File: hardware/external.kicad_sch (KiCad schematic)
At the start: 0 parts

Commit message: :sparkles: external board design
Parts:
- added PC1: ~, KeysDock:POGOPIN-8P-HS, symbol components:POGOPIN-8P-HS
- added R1, R2: 4.7kΩ, KeysDock:R_0402, symbol components:0402,4.7kΩ
- added R3: 10kΩ, KeysDock:R_0402, symbol components:0402,10kΩ
- added R4: 0Ω, KeysDock:R_0402, symbol components:0402,0Ω
- added SW1, SW10, SW11, SW12, SW13, SW14, SW2, SW3, SW4, SW5, SW6, SW7, SW8, SW9: ~, KeysDock:KD-SINGLE-KEY, symbol components:KD_SINGLE_KEY
- added T1: ~, KeysDock:XL4067TS, symbol components:XL4067TS
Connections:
- new net: SW14.H3 (HE_VOUT), T1.2 (Y7)
- new net: SW1.H4 (HE_SLEEP), SW11.H4 (HE_SLEEP), SW13.H4 (HE_SLEEP), SW14.H4 (HE_SLEEP), SW3.H4 (HE_SLEEP), SW5.H4 (HE_SLEEP), SW7.H4 (HE_SLEEP), SW9.H4 (HE_SLEEP)
- new net: R3.2, SW1.H6 (HE_AWAKE), SW10.H6 (HE_AWAKE), SW11.H6 (HE_AWAKE), SW12.H6 (HE_AWAKE), SW13.H6 (HE_AWAKE), SW14.H6 (HE_AWAKE), SW2.H6 (HE_AWAKE), SW3.H6 (HE_AWAKE), SW4.H6 (HE_AWAKE), SW5.H6 (HE_AWAKE), SW6.H6 (HE_AWAKE), SW7.H6 (HE_AWAKE), SW8.H6 (HE_AWAKE), SW9.H6 (HE_AWAKE)
- new net: SW8.H3 (HE_VOUT), T1.19 (Y12)
- new net: SW10.H4 (HE_SLEEP), SW12.H4 (HE_SLEEP), SW2.H4 (HE_SLEEP), SW4.H4 (HE_SLEEP), SW6.H4 (HE_SLEEP), SW8.H4 (HE_SLEEP)
- new net: SW7.H3 (HE_VOUT), T1.6 (Y3)
- new net: R1.1, T1.22 (Y9)
- new net: SW11.H3 (HE_VOUT), T1.4 (Y5)
- new net: SW9.H3 (HE_VOUT), T1.5 (Y4)
- new net: SW2.H3 (HE_VOUT), T1.16 (Y15)
- new net: SW4.H3 (HE_VOUT), T1.17 (Y14)
- new net: SW6.H3 (HE_VOUT), T1.18 (Y13)
- new net: SW10.H3 (HE_VOUT), T1.20 (Y11)
- new net: SW12.H3 (HE_VOUT), T1.21 (Y10)
- new net: R2.1, T1.23 (Y8)
- new net: SW13.H3 (HE_VOUT), T1.3 (Y6)
- new net: SW5.H3 (HE_VOUT), T1.7 (Y2)
- new net: SW3.H3 (HE_VOUT), T1.8 (Y1)
- new net: SW1.H3 (HE_VOUT), T1.9 (Y0)
- new net KEYS_ADC_OUT: PC1.3 (Y3), T1.1 (Z)
- new net KEYS_CH_A: PC1.5 (Y5), T1.10 (A)
- new net KEYS_CH_B: PC1.6 (Y6), T1.11 (B)
- new net KEYS_CH_C: PC1.7 (Y7), T1.14 (C)
- new net KEYS_CH_CE: PC1.4 (Y4), T1.15 (E#)
- new net KEYS_CH_D: PC1.8 (Y8), T1.13 (D)
- new net P,+3.3: PC1.1 (Y1), R1.2, R2.2, R3.1, SW1.H1 (HE_V3.3), SW10.H1 (HE_V3.3), SW11.H1 (HE_V3.3), SW12.H1 (HE_V3.3), SW13.H1 (HE_V3.3), SW14.H1 (HE_V3.3), SW2.H1 (HE_V3.3), SW3.H1 (HE_V3.3), SW4.H1 (HE_V3.3), SW5.H1 (HE_V3.3), SW6.H1 (HE_V3.3), SW7.H1 (HE_V3.3), SW8.H1 (HE_V3.3), SW9.H1 (HE_V3.3), T1.24 (VCC)
- new net P,E: PC1.2 (Y2), R4.2, SW1.H2 (GND), SW1.H5 (GND), SW10.H2 (GND), SW10.H5 (GND), SW11.H2 (GND), SW11.H5 (GND), SW12.H2 (GND), SW12.H5 (GND), SW13.H2 (GND), SW13.H5 (GND), SW14.H2 (GND), SW14.H5 (GND), SW2.H2 (GND), SW2.H5 (GND), SW3.H2 (GND), SW3.H5 (GND), SW4.H2 (GND), SW4.H5 (GND), SW5.H2 (GND), SW5.H5 (GND), SW6.H2 (GND), SW6.H5 (GND), SW7.H2 (GND), SW7.H5 (GND), SW8.H2 (GND), SW8.H5 (GND), SW9.H2 (GND), SW9.H5 (GND), T1.12 (GND)
- new net P,GND: R4.1
- no-connect marks 0 -> 2
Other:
- note added: "GNDA"
- note added: "GNDD"
- note added: "GND_BAT"

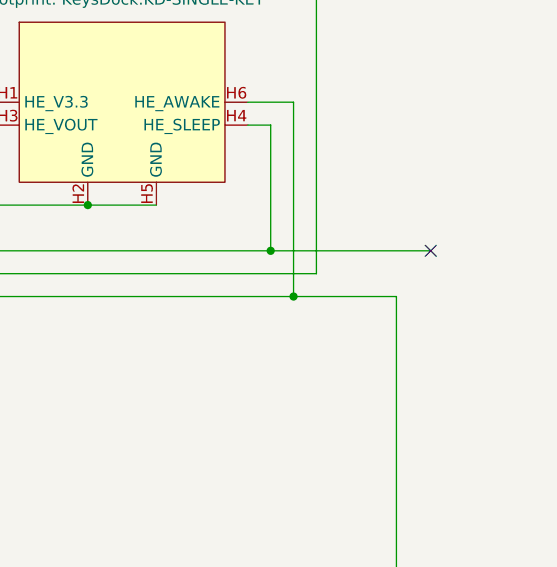
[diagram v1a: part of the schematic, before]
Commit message: :sparkles: finish pcb layout of controller
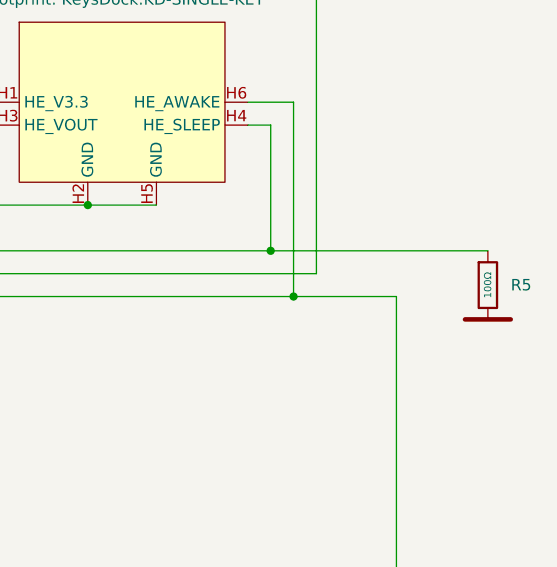
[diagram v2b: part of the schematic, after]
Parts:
- added R5: 100Ω, KeysDock:R_0402, symbol components:0402,100Ω
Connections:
- net P,E: now also R5.2; no longer SW1.H2 (GND), SW1.H5 (GND), SW10.H2 (GND), SW10.H5 (GND), SW11.H2 (GND), SW11.H5 (GND), SW12.H2 (GND), SW12.H5 (GND), SW13.H2 (GND), SW13.H5 (GND), SW14.H2 (GND), SW14.H5 (GND), SW2.H2 (GND), SW2.H5 (GND), SW3.H2 (GND), SW3.H5 (GND), SW4.H2 (GND), SW4.H5 (GND), SW5.H2 (GND), SW5.H5 (GND), SW6.H2 (GND), SW6.H5 (GND), SW7.H2 (GND), SW7.H5 (GND), SW8.H2 (GND), SW8.H5 (GND), SW9.H2 (GND), SW9.H5 (GND), T1.12 (GND)
- net P,GND: now also SW1.H2 (GND), SW1.H5 (GND), SW10.H2 (GND), SW10.H5 (GND), SW11.H2 (GND), SW11.H5 (GND), SW12.H2 (GND), SW12.H5 (GND), SW13.H2 (GND), SW13.H5 (GND), SW14.H2 (GND), SW14.H5 (GND), SW2.H2 (GND), SW2.H5 (GND), SW3.H2 (GND), SW3.H5 (GND), SW4.H2 (GND), SW4.H5 (GND), SW5.H2 (GND), SW5.H5 (GND), SW6.H2 (GND), SW6.H5 (GND), SW7.H2 (GND), SW7.H5 (GND), SW8.H2 (GND), SW8.H5 (GND), SW9.H2 (GND), SW9.H5 (GND), T1.12 (GND)
- net at SW1.H4 (HE_SLEEP), SW11.H4 (HE_SLEEP), SW13.H4 (HE_SLEEP)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: now also R5.1
- no-connect marks 2 -> 1

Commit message: :sparkles: finish all hardware designs
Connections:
- net at R5.1, SW1.H4 (HE_SLEEP), SW11.H4 (HE_SLEEP)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: now also SW10.H4 (HE_SLEEP), SW12.H4 (HE_SLEEP), SW2.H4 (HE_SLEEP), SW4.H4 (HE_SLEEP), SW6.H4 (HE_SLEEP), SW8.H4 (HE_SLEEP)
- no-connect marks 1 -> 0
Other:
- moved on the sheet: R5
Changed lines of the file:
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@@
 	)
 	(junction
+		(at 69.85 80.01)
+		(diameter 0)
+		(color 0 0 0 0)
+	)
+	(junction
 		(at 374.65 85.09)
 		(diameter 0)
@@
 	)
 	(junction
-		(at 100.33 74.93)
+		(at 69.85 158.75)
 		(diameter 0)
 		(color 0 0 0 0)
 	)
 	(junction
-		(at 288.29 153.67)
+		(at 100.33 74.93)
 		(diameter 0)
 		(color 0 0 0 0)
 	)
 	(junction
-		(at 242.57 158.75)
+		(at 288.29 153.67)
 		(diameter 0)
 		(color 0 0 0 0)
 	)
 	(junction
-		(at 285.75 158.75)
+		(at 242.57 158.75)
 		(diameter 0)
 		(color 0 0 0 0)
@@
 		(color 0 0 0 0)
 	)
-	(no_connect
-		(at 307.34 158.75)
-	)
 	(wire
 		(pts
@@
 	(wire
 		(pts
-			(xy 372.11 80.01) (xy 396.24 80.01)
+			(xy 372.11 80.01) (xy 392.43 80.01)
 		)
 		(stroke
@@
 	(wire
 		(pts
-			(xy 285.75 172.72) (xy 285.75 158.75)
-		)
-		(stroke
-			(width 0)
-			(type default)
-		)
-	)
-	(wire
-		(pts
 			(xy 243.84 128.27) (xy 243.84 143.51)
 		)
@@
 	(wire
 		(pts
+			(xy 25.4 158.75) (xy 69.85 158.75)
+		)
+		(stroke
+			(width 0)
+			(type default)
+		)
+	)
+	(wire
+		(pts
 			(xy 217.17 132.08) (xy 217.17 151.13)
 		)
@@
 	(wire
 		(pts
+			(xy 25.4 80.01) (xy 25.4 158.75)
+		)
+		(stroke
+			(width 0)
+			(type default)
+		)
+	)
+	(wire
+		(pts
 			(xy 207.01 156.21) (xy 250.19 156.21)
 		)
@@
 	(wire
 		(pts
+			(xy 69.85 80.01) (xy 25.4 80.01)
+		)
+		(stroke
+			(width 0)
+			(type default)
+		)
+	)
+	(wire
+		(pts
 			(xy 36.83 143.51) (xy 204.47 143.51)
 		)
@@
 	(wire
 		(pts
+			(xy 285.75 158.75) (xy 285.75 172.72)
+		)
+		(stroke
+			(width 0)
+			(type default)
+		)
+	)
+	(wire
+		(pts
 			(xy 288.29 153.67) (xy 288.29 175.26)
 		)
@@
 	(wire
 		(pts
-			(xy 285.75 158.75) (xy 307.34 158.75)
+			(xy 392.43 93.98) (xy 392.43 87.63)
 		)
 		(stroke
@@
 	(symbol
 		(lib_id "PCM_Generic:P,0")
-		(at 396.24 87.63 0)
+		(at 392.43 93.98 0)
 		(unit 1)
 		(exclude_from_sim no)
@@
 		(fields_autoplaced yes)
 		(property "Reference" "#PWR03"
-			(at 400.05 83.82 0)
+			(at 396.24 90.17 0)
 			(effects
 				(font
@@
 		)
 		(property "Value" "P,E"
-			(at 400.05 87.63 0)
+			(at 396.24 93.98 0)
 			(effects
 				(font
@@
 		)
 		(property "Footprint" ""
-			(at 396.24 87.63 0)
+			(at 392.43 93.98 0)
 			(effects
 				(font
@@
 		)
 		(property "Datasheet" ""
-			(at 396.24 87.63 0)
+			(at 392.43 93.98 0)
 			(effects
 				(font
@@
 		)
 		(property "Description" "global node 0; simplified functional (equipotential) bonding (FB); simplified frame/chassis"
-			(at 396.24 87.63 0)
+			(at 392.43 93.98 0)
 			(effects
 				(font
@@
 	(symbol
 		(lib_id "components:0402,100Ω")
-		(at 396.24 83.82 0)
+		(at 392.43 83.82 0)
 		(unit 1)
 		(exclude_from_sim no)
@@
 		(fields_autoplaced yes)
 		(property "Reference" "R5"
-			(at 398.78 83.8199 0)
+			(at 394.97 83.8199 0)
 			(effects
 				(font
@@
 		)
 		(property "Value" "100Ω"
-			(at 396.24 83.82 90)
+			(at 392.43 83.82 90)
 			(do_not_autoplace yes)
 			(effects
@@
 		)
 		(property "Footprint" "KeysDock:R_0402"
-			(at 394.462 83.82 90)
+			(at 390.652 83.82 90)
 			(effects
 				(font
@@
 		)
 		(property "Datasheet" "${KIPRJMOD}/docs/ur-resistors.pdf"
-			(at 396.24 83.82 0)
+			(at 392.43 83.82 0)
 			(effects
 				(font
@@
 		)
 		(property "Description" "62.5mW Thick Film Resistors 50V ±1% ±200ppm/°C 100Ω 0402 Chip Resistor - Surface Mount ROHS"
-			(at 396.24 83.82 0)
+			(at 392.43 83.82 0)
 			(effects
 				(font
@@
 		)
 		(property "LCSC" "C25076"
-			(at 396.24 83.82 0)
+			(at 392.43 83.82 0)
 			(effects
 				(font
@@
 		)
 		(property "Stock" "5907585"
-			(at 396.24 83.82 0)
+			(at 392.43 83.82 0)
 			(effects
 				(font
@@
 		)
 		(property "Price" "0.004USD"
-			(at 396.24 83.82 0)
+			(at 392.43 83.82 0)
 			(effects
 				(font
@@
 		)
 		(property "Process" "SMT"
-			(at 396.24 83.82 0)
+			(at 392.43 83.82 0)
 			(effects
 				(font
@@
 		)
 		(property "Minimum Qty" "20"
-			(at 396.24 83.82 0)
+			(at 392.43 83.82 0)
 			(effects
 				(font
@@
 		)
 		(property "Attrition Qty" "10"
-			(at 396.24 83.82 0)
+			(at 392.43 83.82 0)
 			(effects
 				(font
@@
 		)
 		(property "Class" "Basic Component"
-			(at 396.24 83.82 0)
+			(at 392.43 83.82 0)
 			(effects
 				(font
@@
 		)
 		(property "Category" "Resistors,Chip Resistor - Surface Mount"
-			(at 396.24 83.82 0)
+			(at 392.43 83.82 0)
 			(effects
 				(font
@@
 		)
 		(property "Manufacturer" "UNI-ROYAL(Uniroyal Elec)"
-			(at 396.24 83.82 0)
+			(at 392.43 83.82 0)
 			(effects
 				(font
@@
 		)
 		(property "Part" "0402WGF1000TCE"
-			(at 396.24 83.82 0)
+			(at 392.43 83.82 0)
 			(effects
 				(font
@@
 		)
 		(property "Resistance" "100Ω"
-			(at 396.24 83.82 0)
+			(at 392.43 83.82 0)
 			(effects
 				(font
@@
 		)
 		(property "Power(Watts)" "62.5mW"
-			(at 396.24 83.82 0)
+			(at 392.43 83.82 0)
 			(effects
 				(font
@@
 		)
 		(property "Type" "Thick Film Resistors"
-			(at 396.24 83.82 0)
+			(at 392.43 83.82 0)
 			(effects
 				(font
@@
 		)
 		(property "Overload Voltage (Max)" "50V"
-			(at 396.24 83.82 0)
+			(at 392.43 83.82 0)
 			(effects
 				(font
@@
 		)
 		(property "Operating Temperature Range" "-55°C~+155°C"
-			(at 396.24 83.82 0)
+			(at 392.43 83.82 0)
 			(effects
 				(font
@@
 		)
 		(property "Tolerance" "±1%"
-			(at 396.24 83.82 0)
+			(at 392.43 83.82 0)
 			(effects
 				(font
@@
 		)
 		(property "Temperature Coefficient" "±200ppm/°C"
-			(at 396.24 83.82 0)
+			(at 392.43 83.82 0)
 			(effects
 				(font

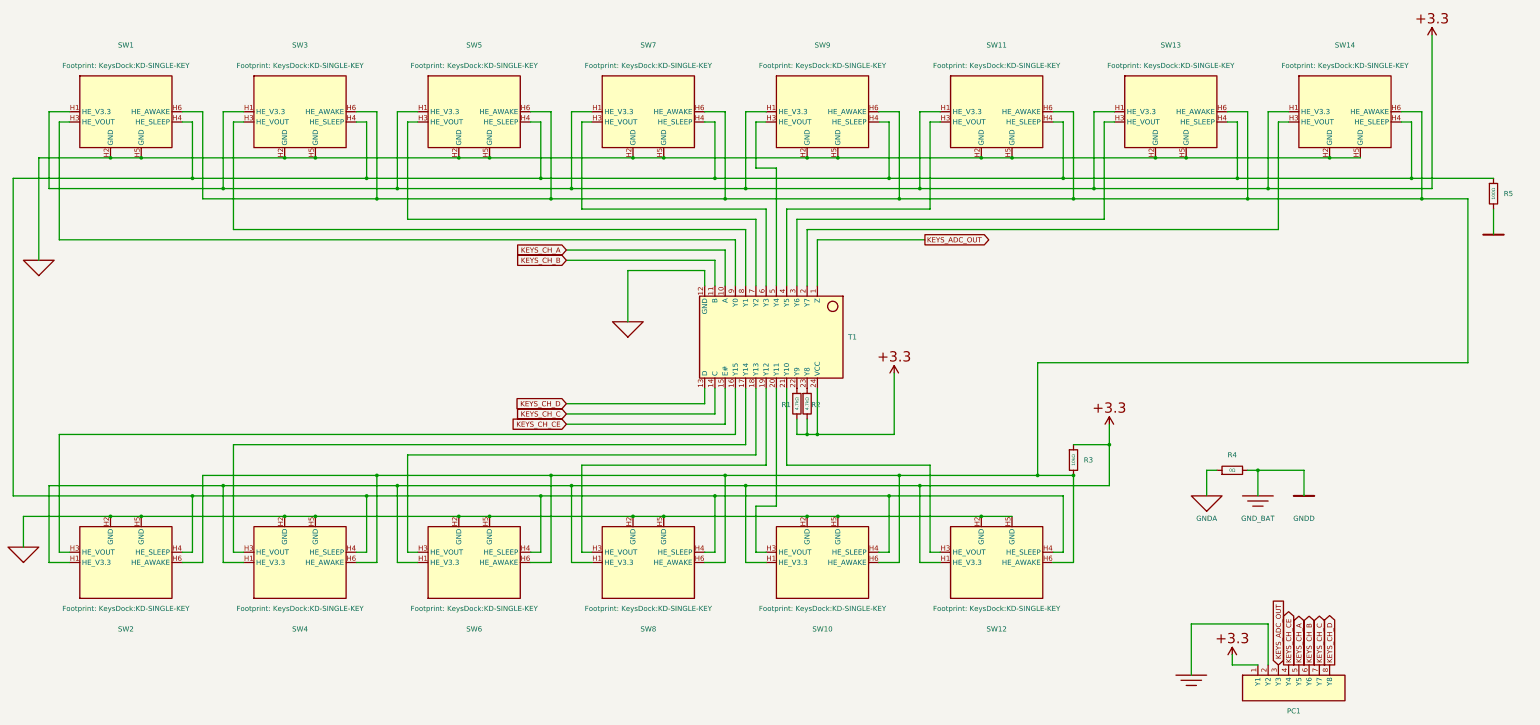
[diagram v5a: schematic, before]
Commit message: :sparkles: add bom table
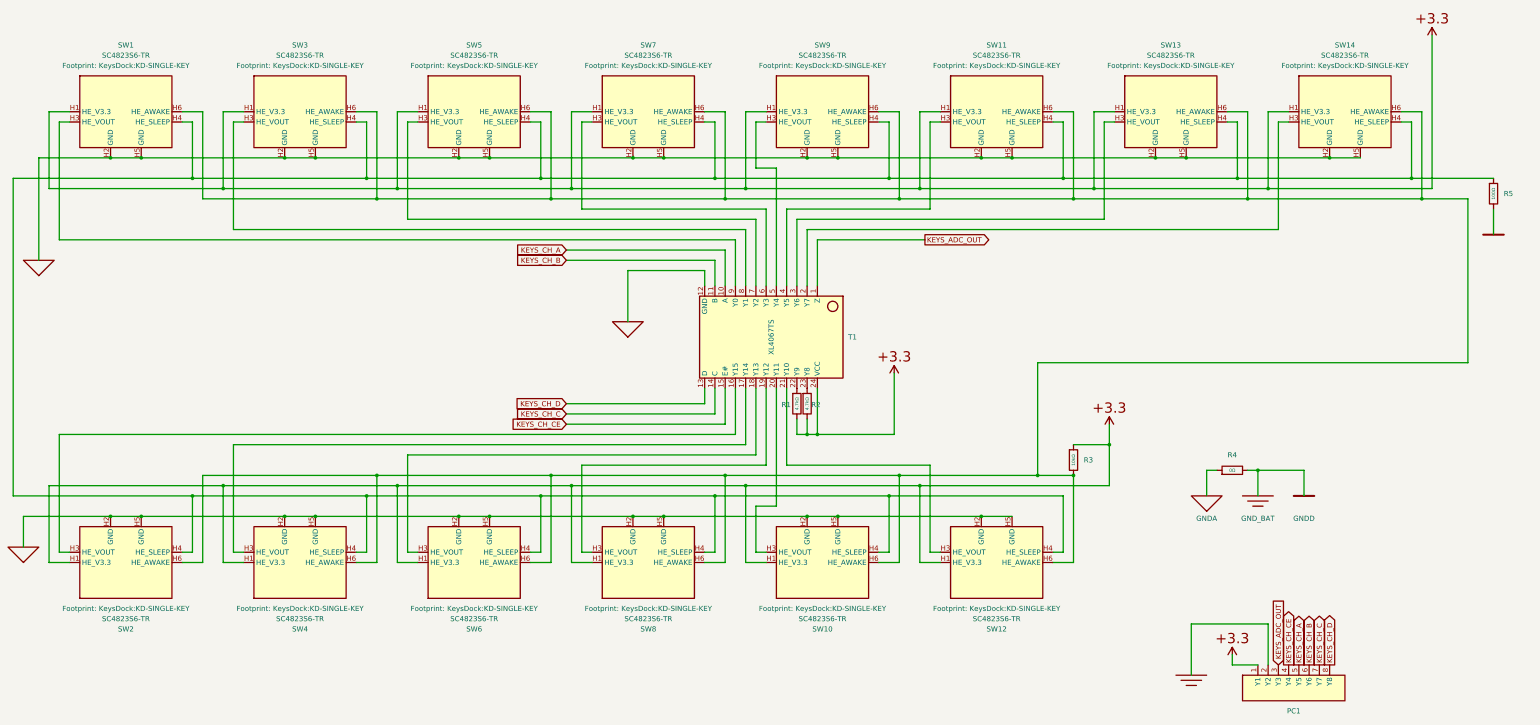
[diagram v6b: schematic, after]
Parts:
- SW1, SW10, SW11, SW12, SW13, SW14, SW2, SW3, SW4, SW5, SW6, SW7, SW8, SW9: value ~ -> SC4823S6-TR; LCSC (none) -> C52021064; Manufacturer (none) -> Semiment(赛卓)
- T1: value ~ -> XL4067TS; LCSC (none) -> C41427445; Manufacturer (none) -> XINLUDA

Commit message: :construction: panelize all boards
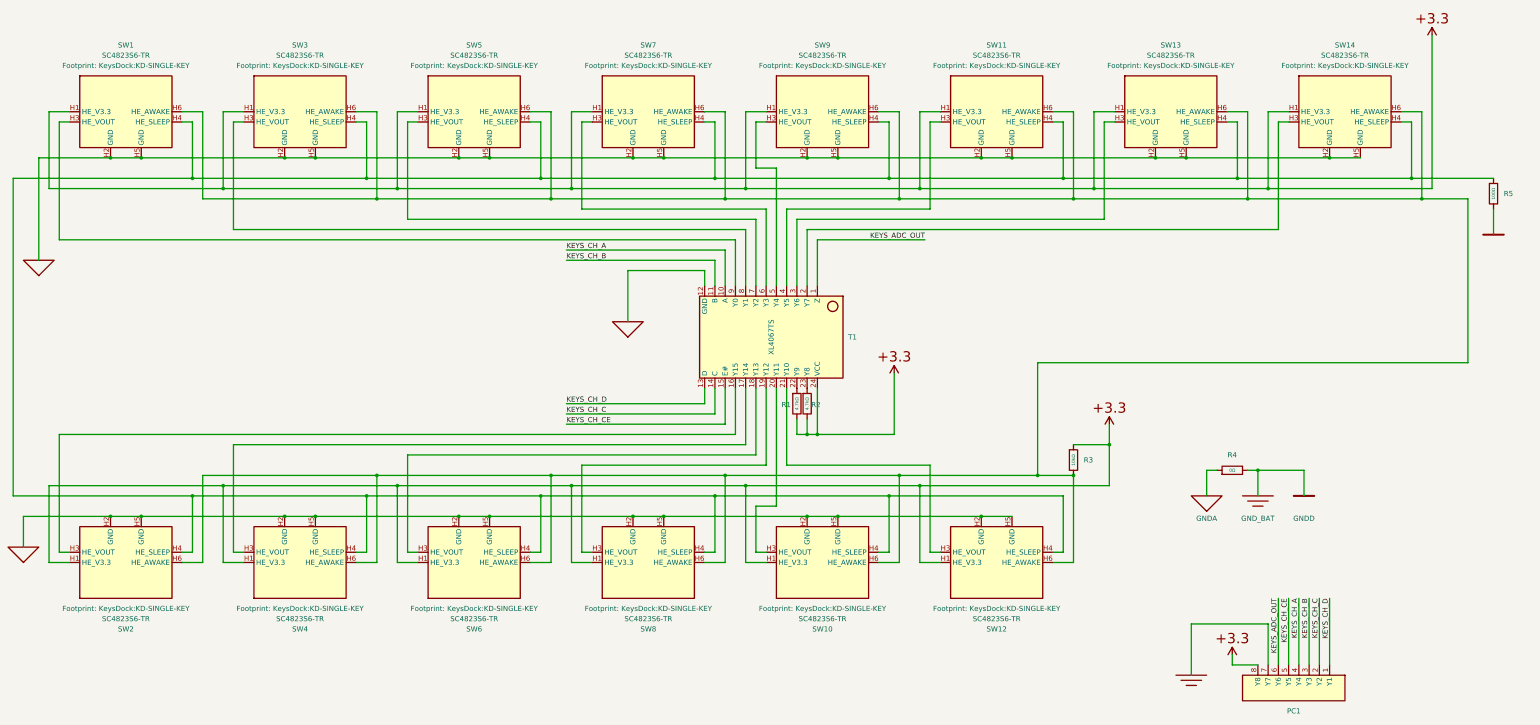
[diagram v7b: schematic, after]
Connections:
- net KEYS_ADC_OUT: now also PC1.6 (Y6); no longer PC1.3 (Y3)
- net KEYS_CH_A: now also PC1.4 (Y4); no longer PC1.5 (Y5)
- net KEYS_CH_B: now also PC1.3 (Y3); no longer PC1.6 (Y6)
- net KEYS_CH_C: now also PC1.2 (Y2); no longer PC1.7 (Y7)
- net KEYS_CH_CE: now also PC1.5 (Y5); no longer PC1.4 (Y4)
- net KEYS_CH_D: now also PC1.1 (Y1); no longer PC1.8 (Y8)
- net P,+3.3: now also PC1.8 (Y8); no longer PC1.1 (Y1)
- net P,E: now also PC1.7 (Y7); no longer PC1.2 (Y2)

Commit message: :arrow_up: update to KiCAD 10.0
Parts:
- PC1: value ~ -> (none)
